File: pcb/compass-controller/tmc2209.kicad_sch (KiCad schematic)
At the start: 18 parts

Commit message: build platform
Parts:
- renumbered C to C20, C to C22, C to C25, J to J3, J to J4, R to R15, R to R21, U to U2
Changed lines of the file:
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@@
 		(on_board yes)
 		(dnp no)
-		(property "Reference" "C"
+		(property "Reference" "C?"
 			(at 166.37 78.74 90)
 			(effects
@@
 					(unit 1)
 				)
+				(path "/4af8dd53-8373-4502-ab9b-bdd4a7fff23c/c3e1c047-9d80-46ca-adc7-2f5e97162326"
+					(reference "C?")
+					(unit 1)
+				)
 			)
 		)
@@
 		(on_board yes)
 		(dnp no)
-		(property "Reference" "R"
+		(property "Reference" "R?"
 			(at 173.99 111.76 0)
 			(effects
@@
 					(unit 1)
 				)
+				(path "/4af8dd53-8373-4502-ab9b-bdd4a7fff23c/c3e1c047-9d80-46ca-adc7-2f5e97162326"
+					(reference "R?")
+					(unit 1)
+				)
 			)
 		)
@@
 		(on_board yes)
 		(dnp no)
-		(property "Reference" "#PWR"
+		(property "Reference" "#PWR?"
 			(at 100.33 83.82 0)
 			(effects
@@
 					(unit 1)
 				)
+				(path "/4af8dd53-8373-4502-ab9b-bdd4a7fff23c/c3e1c047-9d80-46ca-adc7-2f5e97162326"
+					(reference "#PWR?")
+					(unit 1)
+				)
 			)
 		)
@@
 		(on_board yes)
 		(dnp no)
-		(property "Reference" "#PWR"
+		(property "Reference" "#PWR?"
 			(at 175.26 74.93 0)
 			(effects
@@
 				(path "/4af8dd53-8373-4502-ab9b-bdd4a7fff23c/beaee883-de3e-424a-9b2f-6d94b2efca95"
 					(reference "#PWR06")
+					(unit 1)
+				)
+				(path "/4af8dd53-8373-4502-ab9b-bdd4a7fff23c/c3e1c047-9d80-46ca-adc7-2f5e97162326"
+					(reference "#PWR?")
 					(unit 1)
 				)
@@
 		(on_board yes)
 		(dnp no)
-		(property "Reference" "U"
+		(property "Reference" "U?"
 			(at 138.43 91.44 0)
 			(effects
@@
 				(path "/4af8dd53-8373-4502-ab9b-bdd4a7fff23c/beaee883-de3e-424a-9b2f-6d94b2efca95"
 					(reference "U1")
+					(unit 1)
+				)
+				(path "/4af8dd53-8373-4502-ab9b-bdd4a7fff23c/c3e1c047-9d80-46ca-adc7-2f5e97162326"
+					(reference "U?")
 					(unit 1)
 				)
@@
 		(on_board yes)
 		(dnp no)
-		(property "Reference" "J"
+		(property "Reference" "J?"
 			(at 185.42 92.71 0)
 			(effects
@@
 					(unit 1)
 				)
+				(path "/4af8dd53-8373-4502-ab9b-bdd4a7fff23c/c3e1c047-9d80-46ca-adc7-2f5e97162326"
+					(reference "J?")
+					(unit 1)
+				)
 			)
 		)
@@
 		(on_board yes)
 		(dnp no)
-		(property "Reference" "#PWR"
+		(property "Reference" "#PWR?"
 			(at 180.34 78.74 0)
 			(effects
@@
 					(unit 1)
 				)
+				(path "/4af8dd53-8373-4502-ab9b-bdd4a7fff23c/c3e1c047-9d80-46ca-adc7-2f5e97162326"
+					(reference "#PWR?")
+					(unit 1)
+				)
 			)
 		)
@@
 		(on_board yes)
 		(dnp no)
-		(property "Reference" "#PWR"
+		(property "Reference" "#PWR?"
 			(at 181.61 138.43 0)
 			(effects
@@
 					(unit 1)
 				)
+				(path "/4af8dd53-8373-4502-ab9b-bdd4a7fff23c/c3e1c047-9d80-46ca-adc7-2f5e97162326"
+					(reference "#PWR?")
+					(unit 1)
+				)
 			)
 		)
@@
 		(on_board yes)
 		(dnp no)
-		(property "Reference" "C"
+		(property "Reference" "C?"
 			(at 182.88 66.04 0)
 			(effects
@@
 				(path "/4af8dd53-8373-4502-ab9b-bdd4a7fff23c/beaee883-de3e-424a-9b2f-6d94b2efca95"
 					(reference "C18")
+					(unit 1)
+				)
+				(path "/4af8dd53-8373-4502-ab9b-bdd4a7fff23c/c3e1c047-9d80-46ca-adc7-2f5e97162326"
+					(reference "C?")
 					(unit 1)
 				)
@@
 		(on_board yes)
 		(dnp no)
-		(property "Reference" "C"
+		(property "Reference" "C?"
 			(at 116.84 66.04 0)
 			(effects
@@
 				(path "/4af8dd53-8373-4502-ab9b-bdd4a7fff23c/beaee883-de3e-424a-9b2f-6d94b2efca95"
 					(reference "C13")
+					(unit 1)
+				)
+				(path "/4af8dd53-8373-4502-ab9b-bdd4a7fff23c/c3e1c047-9d80-46ca-adc7-2f5e97162326"
+					(reference "C?")
 					(unit 1)
 				)
@@
 		(on_board yes)
 		(dnp no)
-		(property "Reference" "J"
+		(property "Reference" "J?"
 			(at 87.63 96.52 0)
 			(effects
@@
 				(path "/4af8dd53-8373-4502-ab9b-bdd4a7fff23c/beaee883-de3e-424a-9b2f-6d94b2efca95"
 					(reference "J1")
+					(unit 1)
+				)
+				(path "/4af8dd53-8373-4502-ab9b-bdd4a7fff23c/c3e1c047-9d80-46ca-adc7-2f5e97162326"
+					(reference "J?")
 					(unit 1)
 				)
@@
 		(on_board yes)
 		(dnp no)
-		(property "Reference" "R"
+		(property "Reference" "R?"
 			(at 101.6 82.55 90)
 			(effects
@@
 					(unit 1)
 				)
+				(path "/4af8dd53-8373-4502-ab9b-bdd4a7fff23c/c3e1c047-9d80-46ca-adc7-2f5e97162326"
+					(reference "R?")
+					(unit 1)
+				)

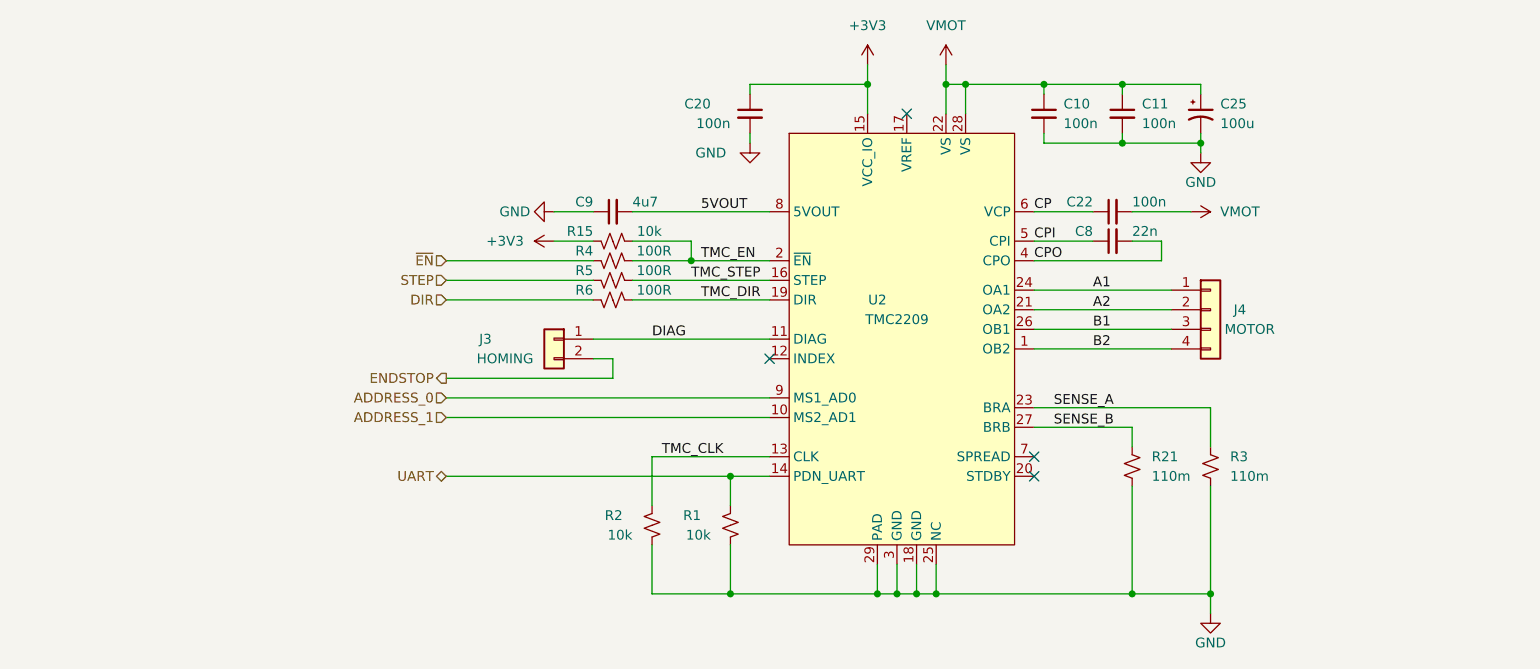
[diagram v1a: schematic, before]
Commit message: finalize schematic, add footprints, start layout
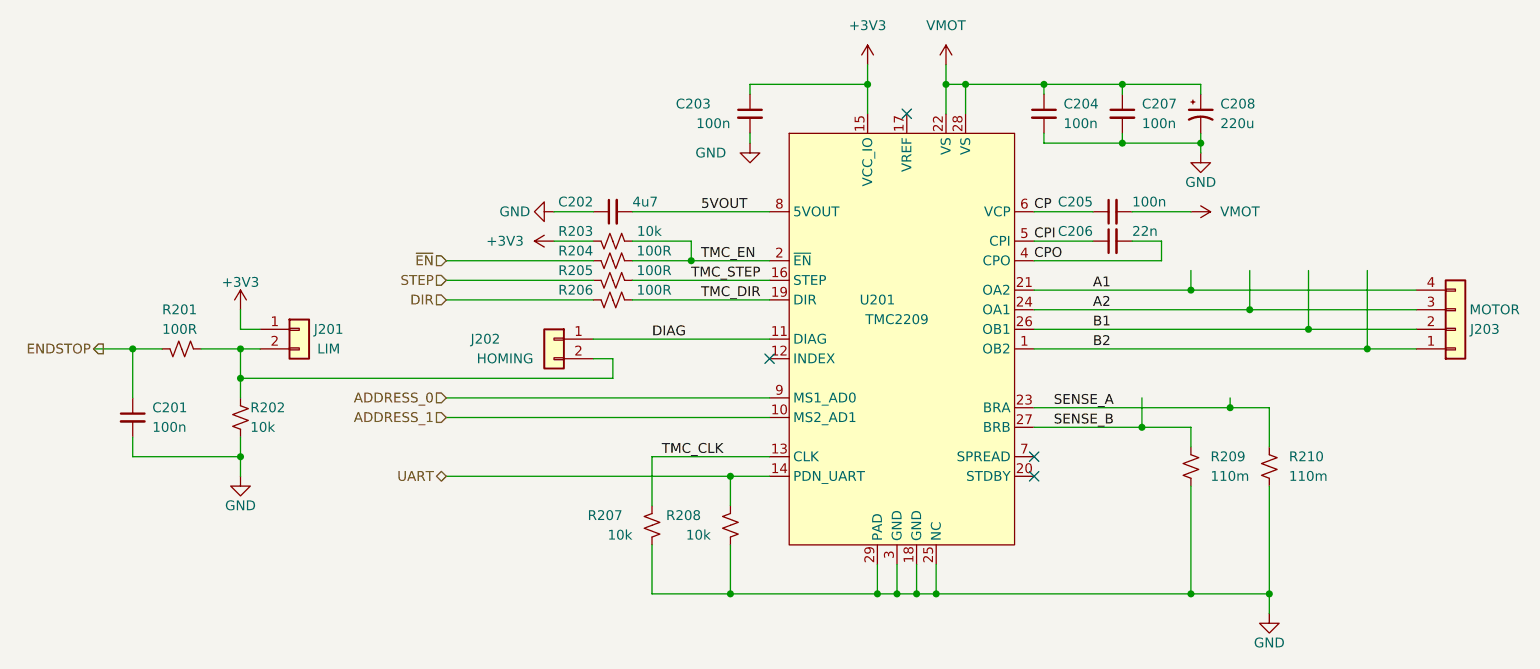
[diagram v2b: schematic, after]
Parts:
- added C201: 100n, Capacitor_SMD:C_0603_1608Metric, symbol Device:C_Small
- added J201: LIM, Connector_JST:JST_XH_B2B-XH-A_1x02_P2.50mm_Vertical, symbol Connector_Generic:Conn_01x02
- added R201: 100R, Resistor_SMD:R_0603_1608Metric, symbol Device:R_Small_US
- added R202: 10k, Resistor_SMD:R_0603_1608Metric, symbol Device:R_Small_US
- C202: renamed from C9; footprint (none) -> Capacitor_SMD:C_0603_1608Metric
- C203: renamed from C20; footprint (none) -> Capacitor_SMD:C_0603_1608Metric
- C204: renamed from C10; footprint (none) -> Capacitor_SMD:C_0603_1608Metric
- C205: renamed from C22; footprint (none) -> Capacitor_SMD:C_0603_1608Metric
- C206: renamed from C8; footprint (none) -> Capacitor_SMD:C_0402_1005Metric
- C207: renamed from C11; footprint (none) -> Capacitor_SMD:C_0603_1608Metric
- C208: renamed from C25; value 100u -> 220u; footprint (none) -> Capacitor_SMD:CP_Elec_5x5.4
- J202: renamed from J3; footprint (none) -> Connector_PinHeader_2.54mm:PinHeader_2x01_P2.54mm_Vertical
- J203: renamed from J4; footprint (none) -> Connector_JST:JST_XH_B4B-XH-AM_1x04_P2.50mm_Vertical
- R203: renamed from R15; footprint (none) -> Resistor_SMD:R_0603_1608Metric
- R204: renamed from R4; footprint (none) -> Resistor_SMD:R_0603_1608Metric
- R205: renamed from R5; footprint (none) -> Resistor_SMD:R_0603_1608Metric
- R206: renamed from R6; footprint (none) -> Resistor_SMD:R_0603_1608Metric
- R207: renamed from R2; footprint (none) -> Resistor_SMD:R_0603_1608Metric
- R208: renamed from R1; footprint (none) -> Resistor_SMD:R_0603_1608Metric
- R209: renamed from R21; footprint (none) -> Resistor_SMD:R_2512_6332Metric
- R210: renamed from R3; footprint (none) -> Resistor_SMD:R_2512_6332Metric
- renumbered U2 to U201
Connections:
- net +3V3: now also J201.1 (Pin_1)
- net A1: now also J203.4 (Pin_4), U201.21 (OA2); no longer J203.1 (Pin_1), U201.24 (OA1)
- net A2: now also J203.3 (Pin_3), U201.24 (OA1); no longer J203.2 (Pin_2), U201.21 (OA2)
- net B1: now also J203.2 (Pin_2); no longer J203.3 (Pin_3)
- net B2: now also J203.1 (Pin_1); no longer J203.4 (Pin_4)
- net ENDSTOP: now also C201.1, R201.1; no longer J202.2 (Pin_2)
- net GND: now also C201.2, R202.2
- new net: J201.2 (Pin_2), J202.2 (Pin_2), R201.2, R202.1
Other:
- moved on the sheet: J203, R209, R210
